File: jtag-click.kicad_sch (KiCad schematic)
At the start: 55 parts, among them J1 Conn_01x08, J2 Conn_01x08, J3 Conn_ARM_JTAG_SWD_20, J4 Conn_ARM_JTAG_SWD_10, Q1 2N7002W, Q2 2N7002W, U1 SN74LVC1T45DCK, U2 SN74LVC1T45DCK, U3 SN74LVC1T45DCK, U4 SN74LVC1T45DCK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

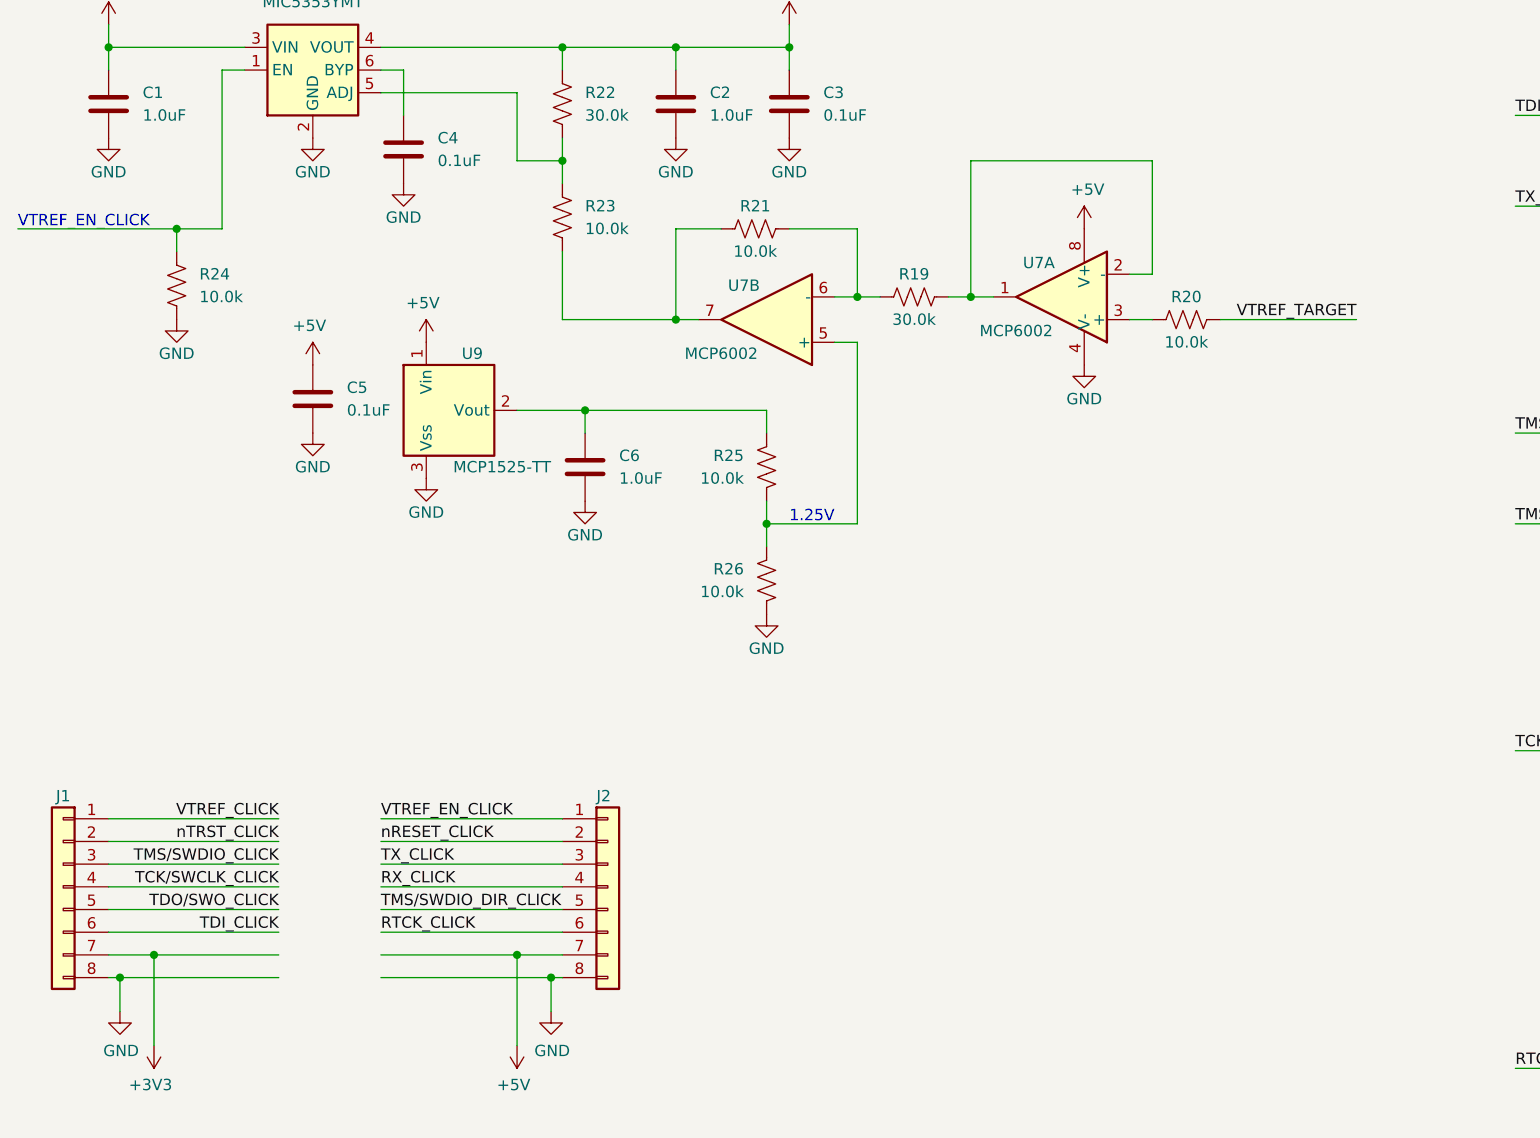
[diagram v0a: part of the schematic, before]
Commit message: Add VTREF_CLICK voltage divider for sensing VTREF
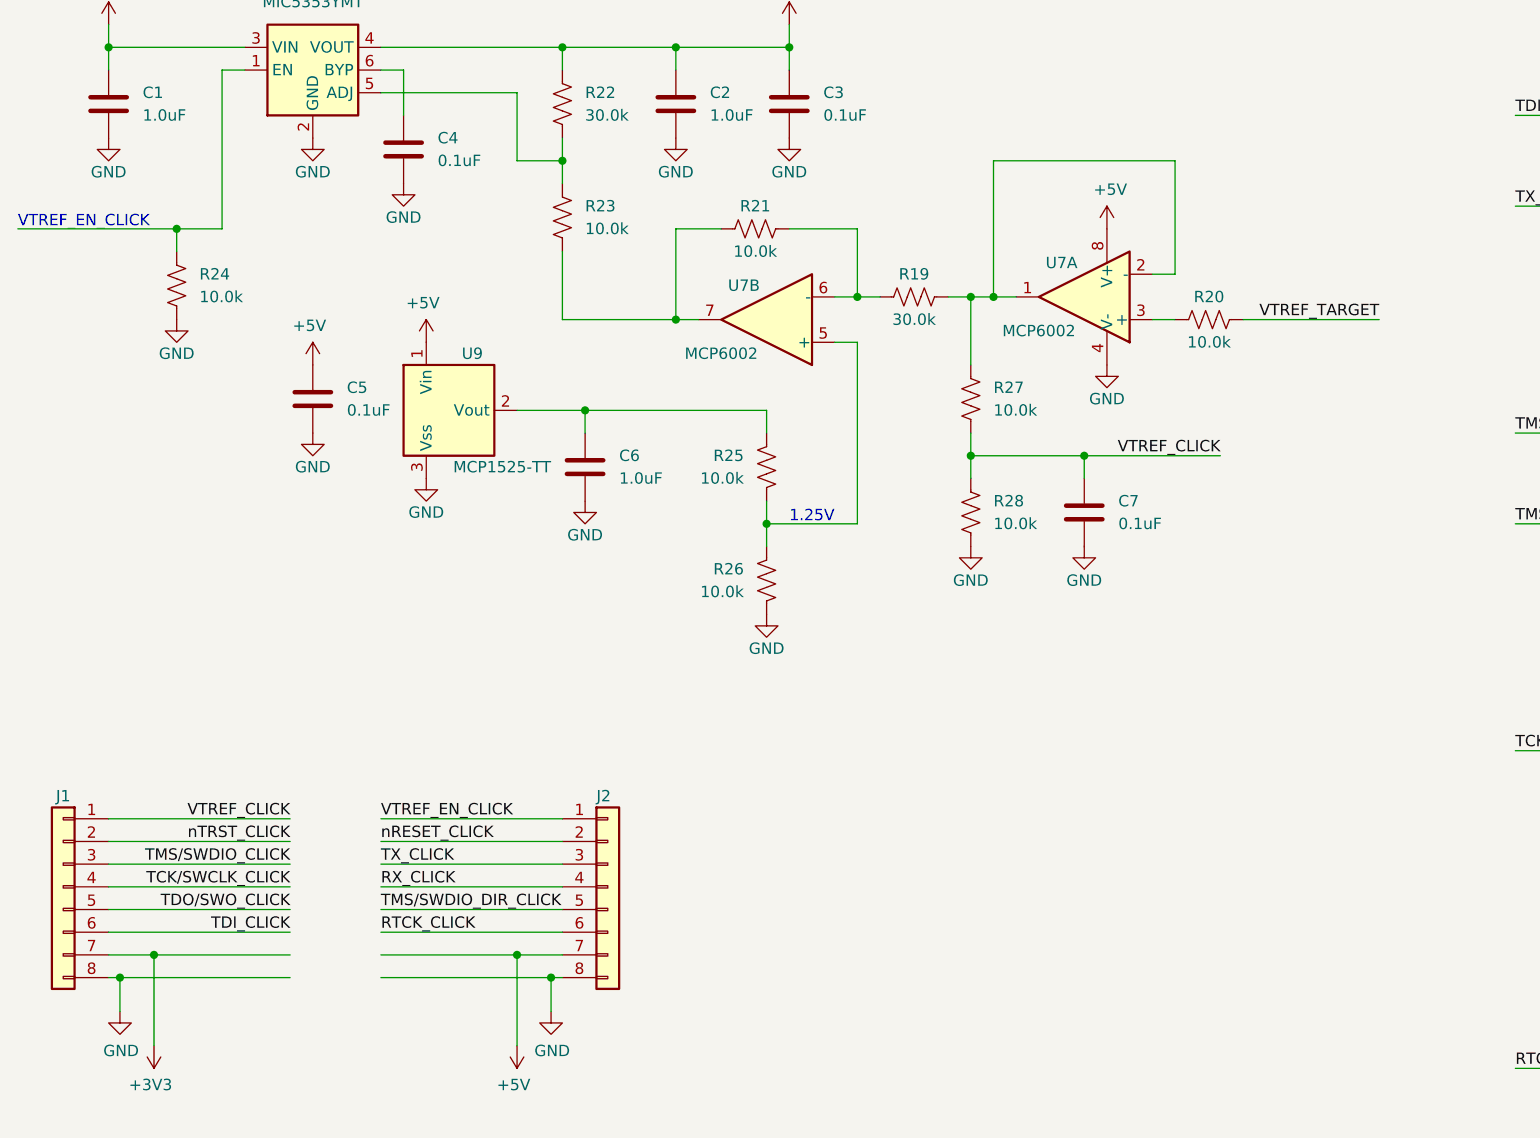
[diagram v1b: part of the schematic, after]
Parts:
- added C7: 0.1uF, Capacitor_SMD:C_0402_1005Metric, symbol Device:C
- added R27, R28: 10.0k, Resistor_SMD:R_0402_1005Metric, symbol Device:R_US
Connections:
- net GND: now also C7.2, R28.2
- net VTREF_CLICK: now also C7.1, R27.2, R28.1
- net at R19.2, U7.1, U7.2 (-): now also R27.1
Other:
- moved on the sheet: R20, U7A

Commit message: Change Vp of clamp diodes to 5V to prevent current flow if VDD is disabled.
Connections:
- net +5V: now also D1.2 (K), D2.2 (K), D3.2 (K), D4.2 (K), D5.2 (K), D6.2 (K), D7.2 (K), D8.2 (K)
- net VDD: no longer D1.2 (K), D2.2 (K), D3.2 (K), D4.2 (K), D5.2 (K), D6.2 (K), D7.2 (K), D8.2 (K)
